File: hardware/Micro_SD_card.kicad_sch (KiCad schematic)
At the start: 5 parts, among them J5 Micro_SD_Card_Det1

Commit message: reorganization of project folders acording to templates
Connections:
- net DET: now reaches J5.9 (DET)
- net +3.3V renamed +3V3
- no-connect marks 3 -> 2
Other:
- moved on the sheet: J5, R16, R17, R18, R19

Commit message: added missing files
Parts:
- R16, R17, R18, R19: Mouser Part Number . -> 71-CRCW0603-4.7K-E3
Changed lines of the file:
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@@
 			)
 		)
-		(property "Datasheet" ""
+		(property "Datasheet" "https://www.vishay.com/docs/20035/dcrcwe3.pdf"
 			(at 134.62 87.63 0)
 			(hide yes)
@@
 			)
 		)
-		(property "Description" "Resistor, small symbol"
+		(property "Description" "Thick Film Resistors - SMD 1/8 Watt 4.7Kohms 1%"
 			(at 134.62 87.63 0)
 			(hide yes)
@@
 			)
 		)
-		(property "Mouser Part Number" "."
+		(property "Mouser Part Number" "71-CRCW0603-4.7K-E3"
 			(at 134.62 80.01 0)
 			(hide yes)
@@
 			)
 		)
-		(property "Datasheet" ""
+		(property "Datasheet" "https://www.vishay.com/docs/20035/dcrcwe3.pdf"
 			(at 118.11 87.63 0)
 			(hide yes)
@@
 			)
 		)
-		(property "Description" "Resistor, small symbol"
+		(property "Description" "Thick Film Resistors - SMD 1/8 Watt 4.7Kohms 1%"
 			(at 118.11 87.63 0)
 			(hide yes)
@@
 			)
 		)
-		(property "Mouser Part Number" "."
+		(property "Mouser Part Number" "71-CRCW0603-4.7K-E3"
 			(at 118.11 80.01 0)
 			(hide yes)
@@
 			)
 		)
-		(property "Datasheet" ""
+		(property "Datasheet" "https://www.vishay.com/docs/20035/dcrcwe3.pdf"
 			(at 123.19 87.63 0)
 			(hide yes)
@@
 			)
 		)
-		(property "Description" "Resistor, small symbol"
+		(property "Description" "Thick Film Resistors - SMD 1/8 Watt 4.7Kohms 1%"
 			(at 123.19 87.63 0)
 			(hide yes)
@@
 			)
 		)
-		(property "Mouser Part Number" "."
+		(property "Mouser Part Number" "71-CRCW0603-4.7K-E3"
 			(at 123.19 80.01 0)
 			(hide yes)
@@
 			)
 		)
-		(property "Datasheet" ""
+		(property "Datasheet" "https://www.vishay.com/docs/20035/dcrcwe3.pdf"
 			(at 128.27 87.63 0)
 			(hide yes)
@@
 			)
 		)
-		(property "Description" "Resistor, small symbol"
+		(property "Description" "Thick Film Resistors - SMD 1/8 Watt 4.7Kohms 1%"
 			(at 128.27 87.63 0)
 			(hide yes)
@@
 			)
 		)
-		(property "Mouser Part Number" "."
+		(property "Mouser Part Number" "71-CRCW0603-4.7K-E3"
 			(at 128.27 80.01 0)
 			(hide yes)

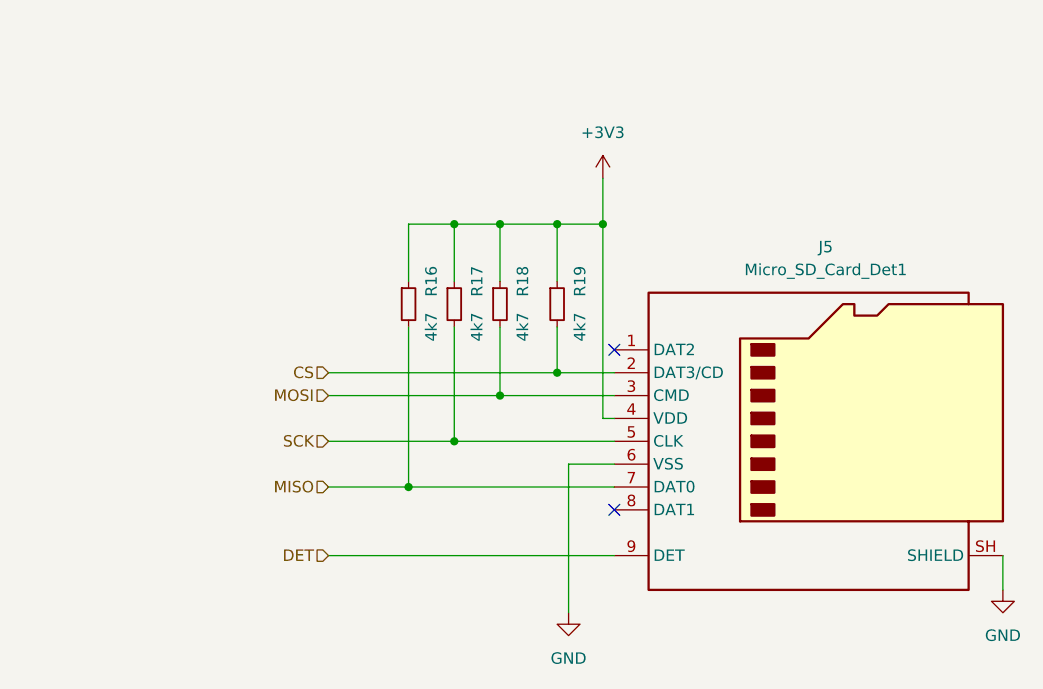
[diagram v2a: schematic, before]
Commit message: reorganize SPI signals into bus
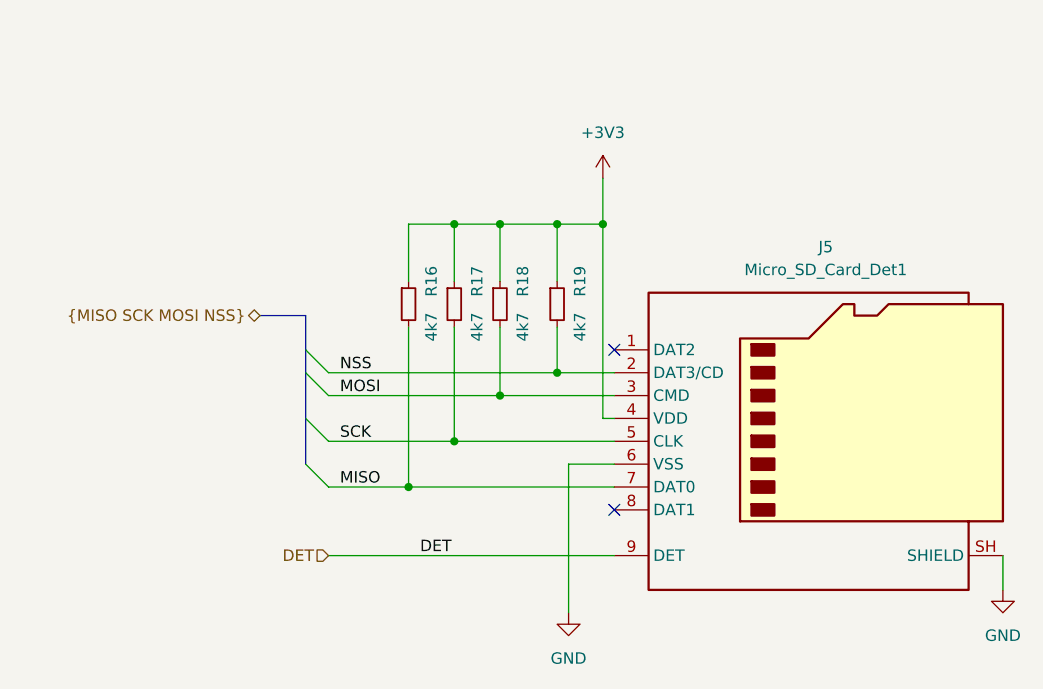
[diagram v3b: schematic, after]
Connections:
- net CS renamed NSS
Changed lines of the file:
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@@
 	(paper "A4")
 	(junction
+		(at 139.7 78.74)
+		(diameter 0)
+		(color 0 0 0 0)
+	)
+	(junction
+		(at 128.27 78.74)
+		(diameter 0)
+		(color 0 0 0 0)
+	)
+	(junction
+		(at 128.27 97.79)
+		(diameter 0)
+		(color 0 0 0 0)
+	)
+	(junction
+		(at 134.62 95.25)
+		(diameter 0)
+		(color 0 0 0 0)
+	)
+	(junction
 		(at 123.19 102.87)
 		(diameter 0)
@@
 	)
 	(junction
-		(at 139.7 78.74)
-		(diameter 0)
-		(color 0 0 0 0)
-	)
-	(junction
-		(at 128.27 78.74)
-		(diameter 0)
-		(color 0 0 0 0)
-	)
-	(junction
-		(at 134.62 95.25)
-		(diameter 0)
-		(color 0 0 0 0)
-	)
-	(junction
-		(at 128.27 97.79)
+		(at 118.11 107.95)
 		(diameter 0)
 		(color 0 0 0 0)
@@
 	(junction
 		(at 134.62 78.74)
-		(diameter 0)
-		(color 0 0 0 0)
-	)
-	(junction
-		(at 118.11 107.95)
 		(diameter 0)
 		(color 0 0 0 0)
@@
 		(at 140.97 92.71)
 	)
+	(bus_entry
+		(at 106.68 105.41)
+		(size 2.54 2.54)
+		(stroke
+			(width 0)
+			(type default)
+		)
+	)
+	(bus_entry
+		(at 106.68 92.71)
+		(size 2.54 2.54)
+		(stroke
+			(width 0)
+			(type default)
+		)
+	)
+	(bus_entry
+		(at 106.68 100.33)
+		(size 2.54 2.54)
+		(stroke
+			(width 0)
+			(type default)
+		)
+	)
+	(bus_entry
+		(at 106.68 95.25)
+		(size 2.54 2.54)
+		(stroke
+			(width 0)
+			(type default)
+		)
+	)
 	(wire
 		(pts
@@
 		)
 	)
+	(bus
+		(pts
+			(xy 106.68 88.9) (xy 101.6 88.9)
+		)
+		(stroke
+			(width 0)
+			(type default)
+		)
+	)
 	(wire
 		(pts
@@
 		)
 	)
+	(bus
+		(pts
+			(xy 106.68 92.71) (xy 106.68 95.25)
+		)
+		(stroke
+			(width 0)
+			(type default)
+		)
+	)
 	(wire
 		(pts
@@
 		)
 	)
+	(bus
+		(pts
+			(xy 106.68 95.25) (xy 106.68 100.33)
+		)
+		(stroke
+			(width 0)
+			(type default)
+		)
+	)
 	(wire
 		(pts
@@
 		)
 	)
+	(bus
+		(pts
+			(xy 106.68 100.33) (xy 106.68 105.41)
+		)
+		(stroke
+			(width 0)
+			(type default)
+		)
+	)
 	(wire
 		(pts
@@
 	(wire
 		(pts
-			(xy 118.11 107.95) (xy 140.97 107.95)
-		)
-		(stroke
-			(width 0)
-			(type default)
-		)
-	)
-	(wire
-		(pts
 			(xy 128.27 78.74) (xy 134.62 78.74)
 		)
@@
 	(wire
 		(pts
-			(xy 109.22 107.95) (xy 118.11 107.95)
-		)
-		(stroke
-			(width 0)
-			(type default)
-		)
-	)
-	(hierarchical_label "MOSI"
-		(shape input)
-		(at 109.22 97.79 180)
-		(effects
-			(font
-				(size 1.27 1.27)
-			)
-			(justify right)
-		)
-	)
-	(hierarchical_label "SCK"
-		(shape input)
-		(at 109.22 102.87 180)
+			(xy 109.22 107.95) (xy 140.97 107.95)
+		)
+		(stroke
+			(width 0)
+			(type default)
+		)
+	)
+	(bus
+		(pts
+			(xy 106.68 88.9) (xy 106.68 92.71)
+		)
+		(stroke
+			(width 0)
+			(type default)
+		)
+	)
+	(label "MOSI"
+		(at 110.49 97.79 0)
+		(effects
+			(font
+				(size 1.27 1.27)
+			)
+			(justify left bottom)
+		)
+	)
+	(label "NSS"
+		(at 110.49 95.25 0)
+		(effects
+			(font
+				(size 1.27 1.27)
+			)
+			(justify left bottom)
+		)
+	)
+	(label "MISO"
+		(at 110.49 107.95 0)
+		(effects
+			(font
+				(size 1.27 1.27)
+			)
+			(justify left bottom)
+		)
+	)
+	(label "DET"
+		(at 119.38 115.57 0)
+		(effects
+			(font
+				(size 1.27 1.27)
+			)
+			(justify left bottom)
+		)
+	)
+	(label "SCK"
+		(at 110.49 102.87 0)
+		(effects
+			(font
+				(size 1.27 1.27)
+			)
+			(justify left bottom)
+		)
+	)
+	(hierarchical_label "{MISO SCK MOSI NSS}"
+		(shape bidirectional)
+		(at 101.6 88.9 180)
 		(effects
 			(font
@@
 		(effects
 			(font
-				(size 1.27 1.27)
-			)
-			(justify right)
-		)
-	)
-	(hierarchical_label "CS"
-		(shape input)
-		(at 109.22 95.25 180)
-		(effects
-			(font
-				(size 1.27 1.27)
-			)
-			(justify right)
-		)
-	)
-	(hierarchical_label "MISO"
-		(shape input)
-		(at 109.22 107.95 180)
-		(effects
-			(font
